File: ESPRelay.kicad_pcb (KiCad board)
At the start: 2 copper layers, 49 x 81 mm, 25 parts, among them J1 RELAY1, J2 RELAY2, J3 SENSOR_1, J4 SENSOR_2, K1 G5Q-1, K2 G5Q-1, Q1 2N3904, Q2 2N3904, U1 NodeMCU_1.0_(ESP-12E), U2 EL817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

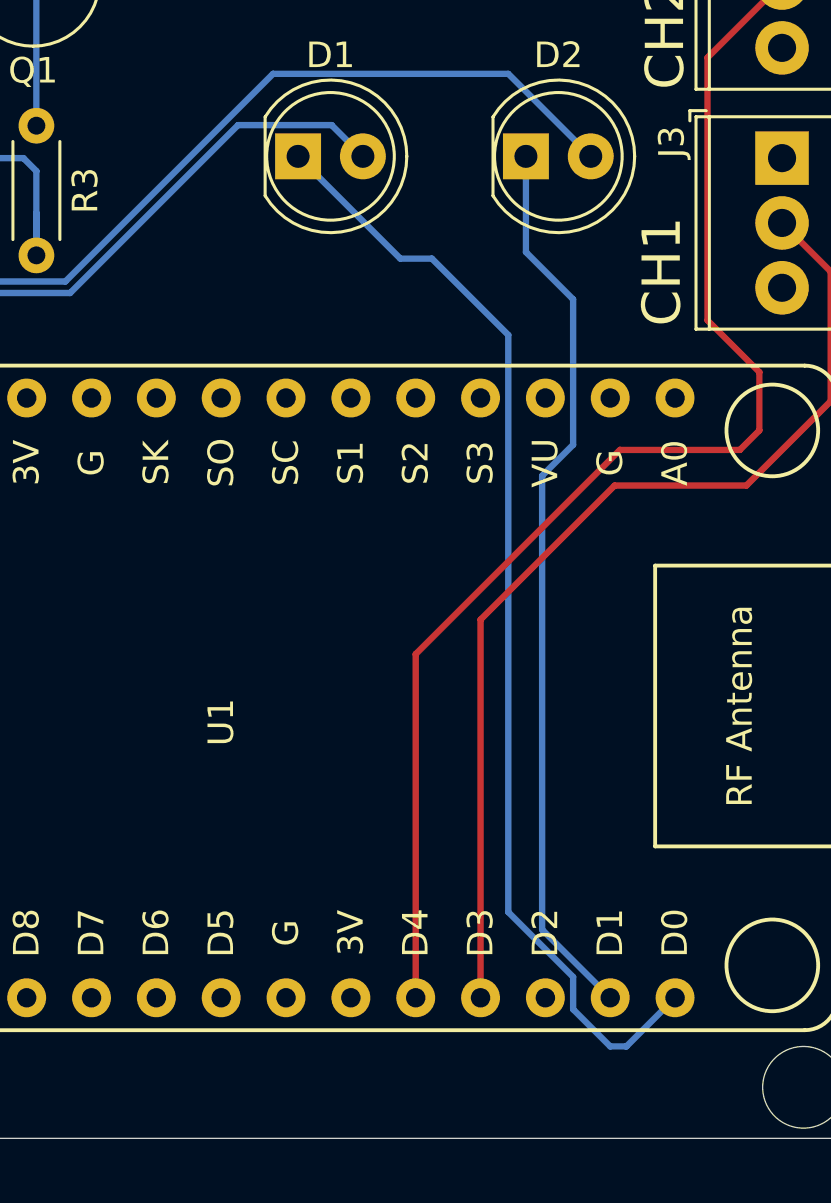
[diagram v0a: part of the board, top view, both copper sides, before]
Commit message: Fixed misconnected sensor inputs
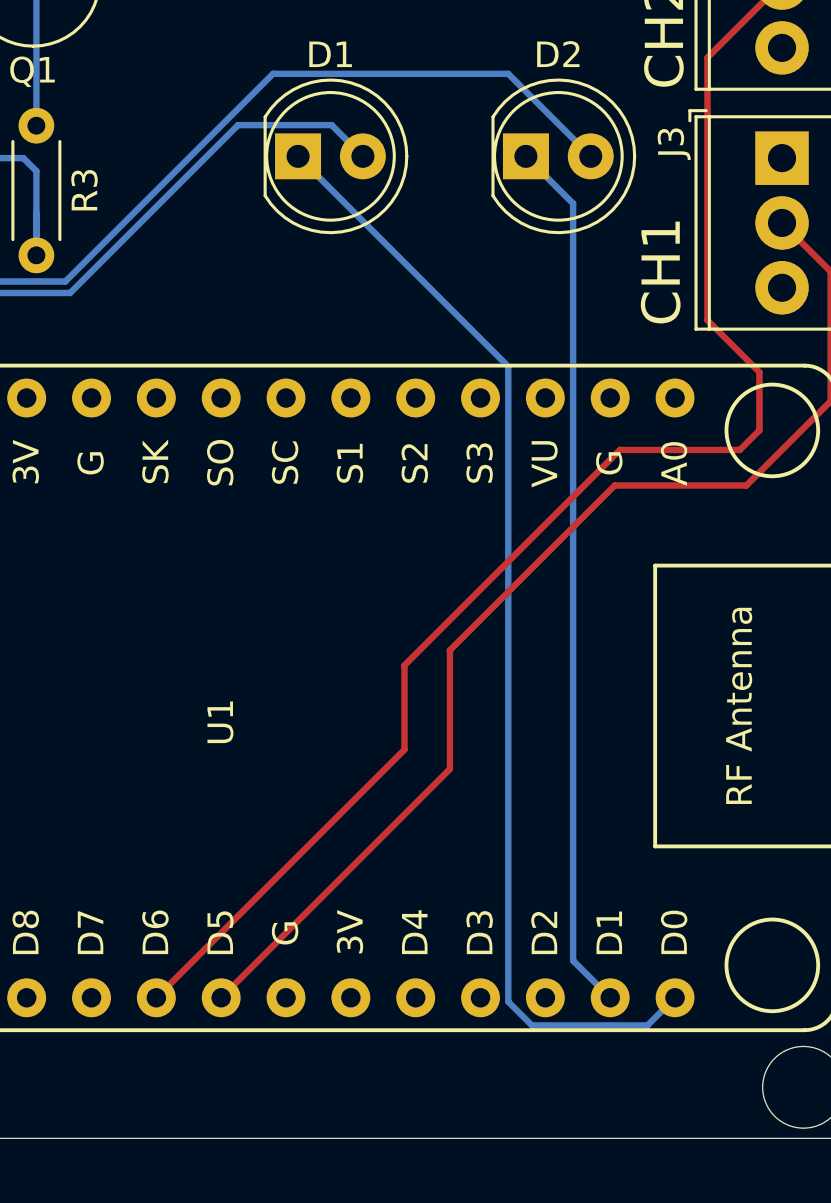
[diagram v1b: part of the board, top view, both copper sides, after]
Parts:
- removed G***: LOGO, Library:Stickman_Logo
- removed REF**: OSHW-Logo_11.4x12mm_SilkScreen, Symbol:OSHW-Logo_11.4x12mm_SilkScreen
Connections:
- U1 pad 22: (no net) -> Net-(J4-Pad2)
- U1 pad 23: (no net) -> Net-(J3-Pad2)
- U1 pad 26: Net-(J4-Pad2) -> (no net)
- U1 pad 27: Net-(J3-Pad2) -> (no net)
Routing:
- net Net-(J4-Pad2): track 50.1 -> 54.3 mm
- net Net-(J3-Pad2): track 39.8 -> 44.1 mm
- net Net-(D2-Pad1): track 35.3 -> 34.3 mm

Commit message: Fix error with relay connections to NodeMCU. Include README.md and git ignore file.
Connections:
- R1 pad 1: VCC -> Net-(R1-Pad1)
- R1 pad 2: Net-(R1-Pad2) -> GND
- R2 pad 1: VCC -> Net-(R2-Pad1)
- R2 pad 2: Net-(R2-Pad2) -> GND
- U1 pad 1: (no net) -> Net-(U1-Pad1)
- U1 pad 11: (no net) -> Net-(U1-Pad11)
- U1 pad 12: (no net) -> Net-(U1-Pad12)
- U1 pad 13: (no net) -> Net-(U1-Pad13)
- U1 pad 18: (no net) -> Net-(U1-Pad18)
- U1 pad 19: (no net) -> Net-(U1-Pad19)
- U1 pad 2: (no net) -> Net-(U1-Pad2)
- U1 pad 20: (no net) -> Net-(U1-Pad20)
- U1 pad 21: (no net) -> Net-(U1-Pad21)
- U1 pad 25: (no net) -> Net-(U1-Pad25)
- U1 pad 26: (no net) -> Net-(U1-Pad26)
- U1 pad 27: (no net) -> Net-(U1-Pad27)
- U1 pad 28: (no net) -> Net-(D2-Pad2)
- U1 pad 29: Net-(D2-Pad1) -> Net-(D1-Pad2)
- U1 pad 3: (no net) -> Net-(U1-Pad3)
- U1 pad 30: Net-(D1-Pad1) -> Net-(U1-Pad30)
- U1 pad 4: (no net) -> Net-(U1-Pad4)
- U1 pad 5: (no net) -> Net-(U1-Pad5)
- U1 pad 6: (no net) -> Net-(U1-Pad6)
- U1 pad 7: (no net) -> Net-(U1-Pad7)
- U1 pad 8: (no net) -> Net-(U1-Pad8)
- U1 pad 9: (no net) -> Net-(U1-Pad9)
- U2 pad 1: Net-(R1-Pad2) -> Net-(D1-Pad1)
- U2 pad 2: Net-(D1-Pad2) -> Net-(R1-Pad1)
- U3 pad 1: Net-(R2-Pad2) -> Net-(D2-Pad1)
- U3 pad 2: Net-(D2-Pad2) -> Net-(R2-Pad1)
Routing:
- net Net-(D2-Pad1): track 34.3 -> 71.2 mm
- net Net-(D2-Pad2): track 61.4 -> 33.7 mm
- net Net-(D1-Pad2): track 66.2 -> 40.3 mm
- net +5V: track 67.4 -> 81.0 mm
- net Net-(R2-Pad2): track 13.3 -> 0.00 mm
- net Net-(R2-Pad1): track 0.00 -> 5.71 mm
- net Net-(R1-Pad1): track 0.00 -> 5.45 mm
- net Net-(R1-Pad2): track 4.69 -> 0.00 mm
- net Net-(D1-Pad1): track 43.9 -> 48.5 mm
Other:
- board text added: "ESP8622 Relay Module V1.2"
- board text removed: "ESP8622 Relay Module V1.1S"
